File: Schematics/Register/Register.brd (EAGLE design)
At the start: 132.1 x 84.8 mm, 42 parts

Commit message: Added register.
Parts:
- removed C1, C2: (no value), rcl:E3,5-8
- removed JP1: (no value), pinhead:2X03
- removed JP4: (no value), pinhead:1X02
- removed X, Y: 74273N, 74ttl-din:DIL20
- removed XB, YB: 74245N, 74ttl-din:DIL20
- removed XL-0, XL-1, XL-2, XL-3, XL-4, XL-5, XL-6, XL-7, YL-0, YL-1, YL-2, YL-3, YL-4, YL-5, YL-6, YL-7: (no value), led:LED5MM
- removed XR-0, XR-1, XR-2, XR-3, XR-4, XR-5, XR-6, XR-7, YR-0, YR-1, YR-2, YR-3, YR-4, YR-5, YR-6, YR-7: (no value), rcl:0207/10
- added CP, OE-A: (no value), pinhead:1X01
- added L0, L1, L2, L3, L4, L5, L6, L7: (no value), led:LED5MM
- added LS245, LS273: (no value), ic-package:SOCKET-20
- added PS: (no value), pinhead:1X02
- added R0, R1, R2, R3, R4, R5, R6, R7: (no value), rcl:0204/7
- moved B-IN 50.9 mm to (4.32, 21.5), turned to 270 degrees
- moved B-OUT 34.6 mm to (37.0, 21.5), turned to 270 degrees
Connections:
- removed net BI-0: B-IN.8, X.3, Y.3
- removed net BI-1: B-IN.7, X.4, Y.4
- removed net BI-2: B-IN.6, X.7, Y.7
- removed net BI-3: B-IN.5, X.8, Y.8
- removed net BI-4: B-IN.4, X.13, Y.13
- removed net BI-5: B-IN.3, X.14, Y.14
- removed net BI-6: B-IN.2, X.17, Y.17
- removed net BI-7: B-IN.1, X.18, Y.18
- removed net BO-0: B-OUT.8, XB.18, YB.18
- removed net BO-1: B-OUT.7, XB.17, YB.17
- removed net BO-2: B-OUT.6, XB.16, YB.16
- removed net BO-3: B-OUT.5, XB.15, YB.15
- removed net BO-4: B-OUT.4, XB.14, YB.14
- removed net BO-5: B-OUT.3, XB.13, YB.13
- removed net BO-6: B-OUT.2, XB.12, YB.12
- removed net BO-7: B-OUT.1, XB.11, YB.11
- removed net N$113: XL-1.A, XR-1.1
- removed net N$116: XL-2.A, XR-2.1
- removed net N$119: XL-3.A, XR-3.1
- removed net N$122: XL-4.A, XR-4.1
- removed net N$125: XL-5.A, XR-5.1
- removed net N$128: XL-6.A, XR-6.1
- removed net N$131: XL-7.A, XR-7.1
- removed net N$134: YL-0.A, YR-0.1
- removed net N$137: YL-1.A, YR-1.1
- removed net N$140: YL-2.A, YR-2.1
- removed net N$143: YL-3.A, YR-3.1
- removed net N$146: YL-4.A, YR-4.1
- removed net N$149: YL-5.A, YR-5.1
- removed net N$152: YL-6.A, YR-6.1
- removed net N$155: YL-7.A, YR-7.1
- removed net N$2: XL-0.A, XR-0.1
- removed net X-0: X.2, XB.2, XR-0.2
- removed net X-1: X.5, XB.3, XR-1.2
- removed net X-2: X.6, XB.4, XR-2.2
- removed net X-3: X.9, XB.5, XR-3.2
- removed net X-4: X.12, XB.6, XR-4.2
- removed net X-5: X.15, XB.7, XR-5.2
- removed net X-6: X.16, XB.8, XR-6.2
- removed net X-7: X.19, XB.9, XR-7.2
- removed net X-B: JP1.5, XB.19
- removed net X-CLR: JP1.1, X.1
- removed net X-CP: JP1.3, X.11
- removed net Y-0: Y.2, YB.2, YR-0.2
- removed net Y-1: Y.5, YB.3, YR-1.2
- removed net Y-2: Y.6, YB.4, YR-2.2
- removed net Y-3: Y.9, YB.5, YR-3.2
- removed net Y-4: Y.12, YB.6, YR-4.2
- removed net Y-5: Y.15, YB.7, YR-5.2
- removed net Y-6: Y.16, YB.8, YR-6.2
- removed net Y-7: Y.19, YB.9, YR-7.2
- removed net Y-B: JP1.2, YB.19
- removed net Y-CLR: JP1.4, Y.1
- removed net Y-CP: JP1.6, Y.11
- new net BO0: B-OUT.8, LS245.11
- new net BO1: B-OUT.7, LS245.12
- new net BO2: B-OUT.6, LS245.13
- new net BO3: B-OUT.5, LS245.14
- new net BO4: B-OUT.4, LS245.15
- new net BO5: B-OUT.3, LS245.16
- new net BO6: B-OUT.2, LS245.17
- new net BO7: B-OUT.1, LS245.18
- new net CP: CP.1, LS273.11
- new net D0: B-IN.1, LS273.3
- new net D1: B-IN.2, LS273.4
- new net D2: B-IN.3, LS273.7
- new net D3: B-IN.4, LS273.8
- new net D4: B-IN.5, LS273.13
- new net D5: B-IN.6, LS273.14
- new net D6: B-IN.7, LS273.17
- new net D7: B-IN.8, LS273.18
- new net N$1: L7.A, R7.1
- new net N$10: L1.A, R1.1
- new net N$11: L0.A, R0.1
- new net N$18: LS245.19, OE-A.1
- new net N$5: L6.A, R6.1
- new net N$6: L5.A, R5.1
- new net N$7: L4.A, R4.1
- new net N$8: L3.A, R3.1
- new net N$9: L2.A, R2.1
- new net Q0: LS245.9, LS273.2, R0.2
- new net Q1: LS245.8, LS273.5, R1.2
- new net Q2: LS245.7, LS273.6, R2.2
- new net Q3: LS245.6, LS273.9, R3.2
- new net Q4: LS245.5, LS273.12, R4.2
- new net Q5: LS245.4, LS273.15, R5.2
- new net Q6: LS245.3, LS273.16, R6.2
- new net Q7: LS245.2, LS273.19, R7.2
- net GND: now also L0.K, L1.K, L2.K, L3.K, L4.K, L5.K, L6.K, L7.K, LS245.10, LS273.10, PS.1; no longer C1.-, C2.-, JP4.2, X.10, XB.10, XL-0.K, XL-1.K, XL-2.K, XL-3.K, XL-4.K, XL-5.K, XL-6.K, XL-7.K, Y.10, YB.10, YL-0.K, YL-1.K, YL-2.K, YL-3.K, YL-4.K, YL-5.K, YL-6.K, YL-7.K
- net VCC: now also LS245.1, LS245.20, LS273.1, LS273.20, PS.2; no longer C1.+, C2.+, JP4.1, X.20, XB.1, XB.20, Y.20, YB.1, YB.20
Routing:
- net BI-1: track 163.3 -> 0.00 mm
- net Y-CLR: track 160.6 -> 0.00 mm, vias 5 -> 0
- net GND: track 248.4 -> 93.5 mm, vias 2 -> 0
- net BO-7: track 153.7 -> 0.00 mm, vias 2 -> 0
- net BO-6: track 151.1 -> 0.00 mm, vias 2 -> 0
- net BI-2: track 149.0 -> 0.00 mm
- net BI-0: track 148.7 -> 0.00 mm
- net BO-5: track 148.6 -> 0.00 mm, vias 2 -> 0
- net BO-4: track 146.0 -> 0.00 mm, vias 2 -> 0
- net BO-3: track 143.5 -> 0.00 mm, vias 2 -> 0
- net BI-6: track 142.5 -> 0.00 mm, vias 5 -> 0
- net BI-3: track 141.8 -> 0.00 mm
- net BO-2: track 141.0 -> 0.00 mm, vias 2 -> 0
- net BI-4: track 139.9 -> 0.00 mm, vias 3 -> 0
- net BO-1: track 138.4 -> 0.00 mm, vias 2 -> 0
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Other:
- board size 132.1 x 84.8 mm -> 40.1 x 49.6 mm
- board text added: "H"
- board text added: "L"
- board text removed: "X"
- board text removed: "X, Y registers."
- board text removed: "Y"

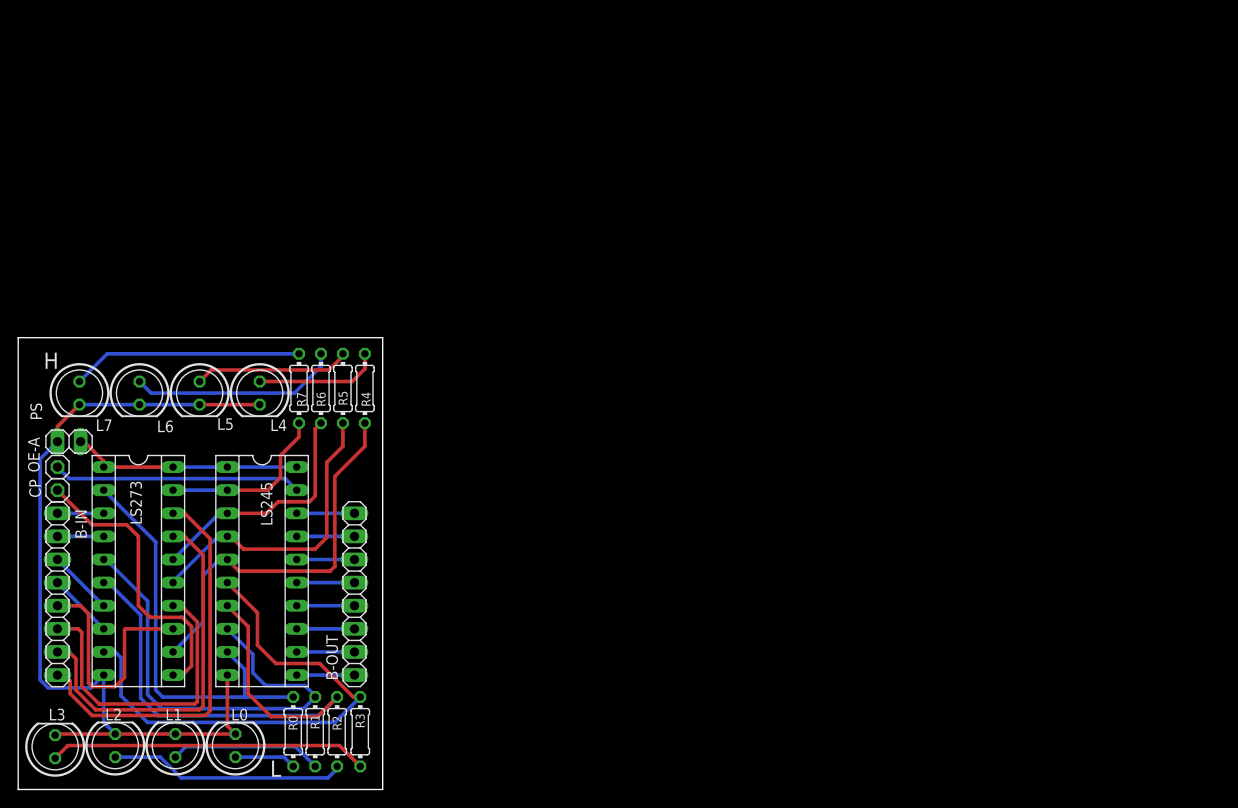
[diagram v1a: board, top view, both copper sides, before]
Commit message: Register, PC, RAM will be solid board not modules, brd is pretty simple.
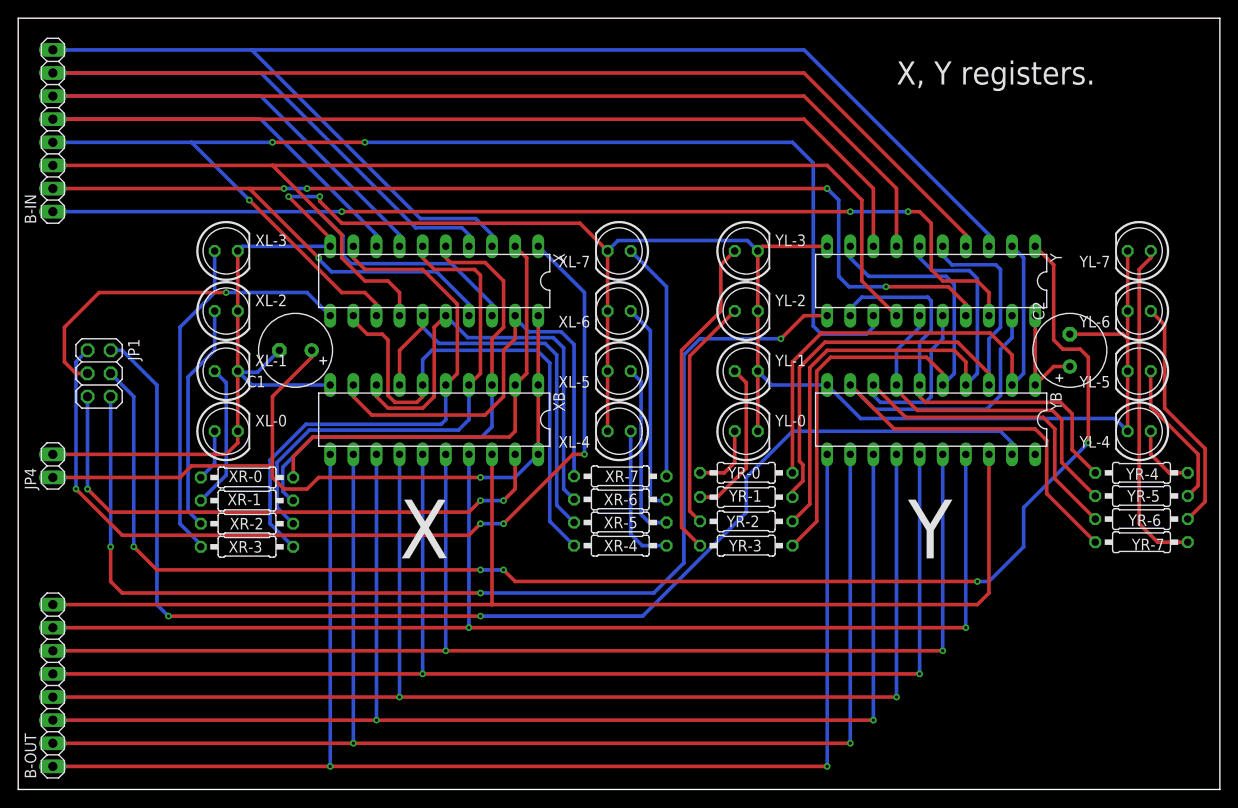
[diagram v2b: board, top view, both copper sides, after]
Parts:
- removed CP, OE-A: (no value), pinhead:1X01
- removed L0, L1, L2, L3, L4, L5, L6, L7: (no value), led:LED5MM
- removed LS245, LS273: (no value), ic-package:SOCKET-20
- removed PS: (no value), pinhead:1X02
- removed R0, R1, R2, R3, R4, R5, R6, R7: (no value), rcl:0204/7
- added C1, C2: (no value), rcl:E3,5-8
- added JP1: (no value), pinhead:2X03
- added JP4: (no value), pinhead:1X02
- added X, Y: 74273N, 74ttl-din:DIL20
- added XB, YB: 74245N, 74ttl-din:DIL20
- added XL-0, XL-1, XL-2, XL-3, XL-4, XL-5, XL-6, XL-7, YL-0, YL-1, YL-2, YL-3, YL-4, YL-5, YL-6, YL-7: (no value), led:LED5MM
- added XR-0, XR-1, XR-2, XR-3, XR-4, XR-5, XR-6, XR-7, YR-0, YR-1, YR-2, YR-3, YR-4, YR-5, YR-6, YR-7: (no value), rcl:0207/10
- moved B-IN 50.9 mm to (3.81, 72.4), turned to 90 degrees
- moved B-OUT 34.6 mm to (3.81, 11.4), turned to 90 degrees
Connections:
- removed net BO0: B-OUT.8, LS245.11
- removed net BO1: B-OUT.7, LS245.12
- removed net BO2: B-OUT.6, LS245.13
- removed net BO3: B-OUT.5, LS245.14
- removed net BO4: B-OUT.4, LS245.15
- removed net BO5: B-OUT.3, LS245.16
- removed net BO6: B-OUT.2, LS245.17
- removed net BO7: B-OUT.1, LS245.18
- removed net CP: CP.1, LS273.11
- removed net D0: B-IN.1, LS273.3
- removed net D1: B-IN.2, LS273.4
- removed net D2: B-IN.3, LS273.7
- removed net D3: B-IN.4, LS273.8
- removed net D4: B-IN.5, LS273.13
- removed net D5: B-IN.6, LS273.14
- removed net D6: B-IN.7, LS273.17
- removed net D7: B-IN.8, LS273.18
- removed net N$1: L7.A, R7.1
- removed net N$10: L1.A, R1.1
- removed net N$11: L0.A, R0.1
- removed net N$18: LS245.19, OE-A.1
- removed net N$5: L6.A, R6.1
- removed net N$6: L5.A, R5.1
- removed net N$7: L4.A, R4.1
- removed net N$8: L3.A, R3.1
- removed net N$9: L2.A, R2.1
- removed net Q0: LS245.9, LS273.2, R0.2
- removed net Q1: LS245.8, LS273.5, R1.2
- removed net Q2: LS245.7, LS273.6, R2.2
- removed net Q3: LS245.6, LS273.9, R3.2
- removed net Q4: LS245.5, LS273.12, R4.2
- removed net Q5: LS245.4, LS273.15, R5.2
- removed net Q6: LS245.3, LS273.16, R6.2
- removed net Q7: LS245.2, LS273.19, R7.2
- new net BI-0: B-IN.8, X.3, Y.3
- new net BI-1: B-IN.7, X.4, Y.4
- new net BI-2: B-IN.6, X.7, Y.7
- new net BI-3: B-IN.5, X.8, Y.8
- new net BI-4: B-IN.4, X.13, Y.13
- new net BI-5: B-IN.3, X.14, Y.14
- new net BI-6: B-IN.2, X.17, Y.17
- new net BI-7: B-IN.1, X.18, Y.18
- new net BO-0: B-OUT.8, XB.18, YB.18
- new net BO-1: B-OUT.7, XB.17, YB.17
- new net BO-2: B-OUT.6, XB.16, YB.16
- new net BO-3: B-OUT.5, XB.15, YB.15
- new net BO-4: B-OUT.4, XB.14, YB.14
- new net BO-5: B-OUT.3, XB.13, YB.13
- new net BO-6: B-OUT.2, XB.12, YB.12
- new net BO-7: B-OUT.1, XB.11, YB.11
- new net N$113: XL-1.A, XR-1.1
- new net N$116: XL-2.A, XR-2.1
- new net N$119: XL-3.A, XR-3.1
- new net N$122: XL-4.A, XR-4.1
- new net N$125: XL-5.A, XR-5.1
- new net N$128: XL-6.A, XR-6.1
- new net N$131: XL-7.A, XR-7.1
- new net N$134: YL-0.A, YR-0.1
- new net N$137: YL-1.A, YR-1.1
- new net N$140: YL-2.A, YR-2.1
- new net N$143: YL-3.A, YR-3.1
- new net N$146: YL-4.A, YR-4.1
- new net N$149: YL-5.A, YR-5.1
- new net N$152: YL-6.A, YR-6.1
- new net N$155: YL-7.A, YR-7.1
- new net N$2: XL-0.A, XR-0.1
- new net X-0: X.2, XB.2, XR-0.2
- new net X-1: X.5, XB.3, XR-1.2
- new net X-2: X.6, XB.4, XR-2.2
- new net X-3: X.9, XB.5, XR-3.2
- new net X-4: X.12, XB.6, XR-4.2
- new net X-5: X.15, XB.7, XR-5.2
- new net X-6: X.16, XB.8, XR-6.2
- new net X-7: X.19, XB.9, XR-7.2
- new net X-B: JP1.5, XB.19
- new net X-CLR: JP1.1, X.1
- new net X-CP: JP1.3, X.11
- new net Y-0: Y.2, YB.2, YR-0.2
- new net Y-1: Y.5, YB.3, YR-1.2
- new net Y-2: Y.6, YB.4, YR-2.2
- new net Y-3: Y.9, YB.5, YR-3.2
- new net Y-4: Y.12, YB.6, YR-4.2
- new net Y-5: Y.15, YB.7, YR-5.2
- new net Y-6: Y.16, YB.8, YR-6.2
- new net Y-7: Y.19, YB.9, YR-7.2
- new net Y-B: JP1.2, YB.19
- new net Y-CLR: JP1.4, Y.1
- new net Y-CP: JP1.6, Y.11
- net GND: now also C1.-, C2.-, JP4.2, X.10, XB.10, XL-0.K, XL-1.K, XL-2.K, XL-3.K, XL-4.K, XL-5.K, XL-6.K, XL-7.K, Y.10, YB.10, YL-0.K, YL-1.K, YL-2.K, YL-3.K, YL-4.K, YL-5.K, YL-6.K, YL-7.K; no longer L0.K, L1.K, L2.K, L3.K, L4.K, L5.K, L6.K, L7.K, LS245.10, LS273.10, PS.1
- net VCC: now also C1.+, C2.+, JP4.1, X.20, XB.1, XB.20, Y.20, YB.1, YB.20; no longer LS245.1, LS245.20, LS273.1, LS273.20, PS.2
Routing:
- net BI-1: track 0.00 -> 163.3 mm
- net Y-CLR: track 0.00 -> 160.6 mm, vias 0 -> 5
- net GND: track 93.5 -> 248.4 mm, vias 0 -> 2
- net BO-7: track 0.00 -> 153.7 mm, vias 0 -> 2
- net BO-6: track 0.00 -> 151.1 mm, vias 0 -> 2
- net BI-2: track 0.00 -> 149.0 mm
- net BI-0: track 0.00 -> 148.7 mm
- net BO-5: track 0.00 -> 148.6 mm, vias 0 -> 2
- net BO-4: track 0.00 -> 146.0 mm, vias 0 -> 2
- net BO-3: track 0.00 -> 143.5 mm, vias 0 -> 2
- net BI-6: track 0.00 -> 142.5 mm, vias 0 -> 5
- net BI-3: track 0.00 -> 141.8 mm
- net BO-2: track 0.00 -> 141.0 mm, vias 0 -> 2
- net BI-4: track 0.00 -> 139.9 mm, vias 0 -> 3
- net BO-1: track 0.00 -> 138.4 mm, vias 0 -> 2
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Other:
- board size 40.1 x 49.6 mm -> 132.1 x 84.8 mm
- board text added: "X"
- board text added: "X, Y registers."
- board text added: "Y"
- board text removed: "H"
- board text removed: "L"
